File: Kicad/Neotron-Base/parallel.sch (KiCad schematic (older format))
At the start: 11 parts, among them J501 Conn_02x13_Header, U501 MCP23S17_SP

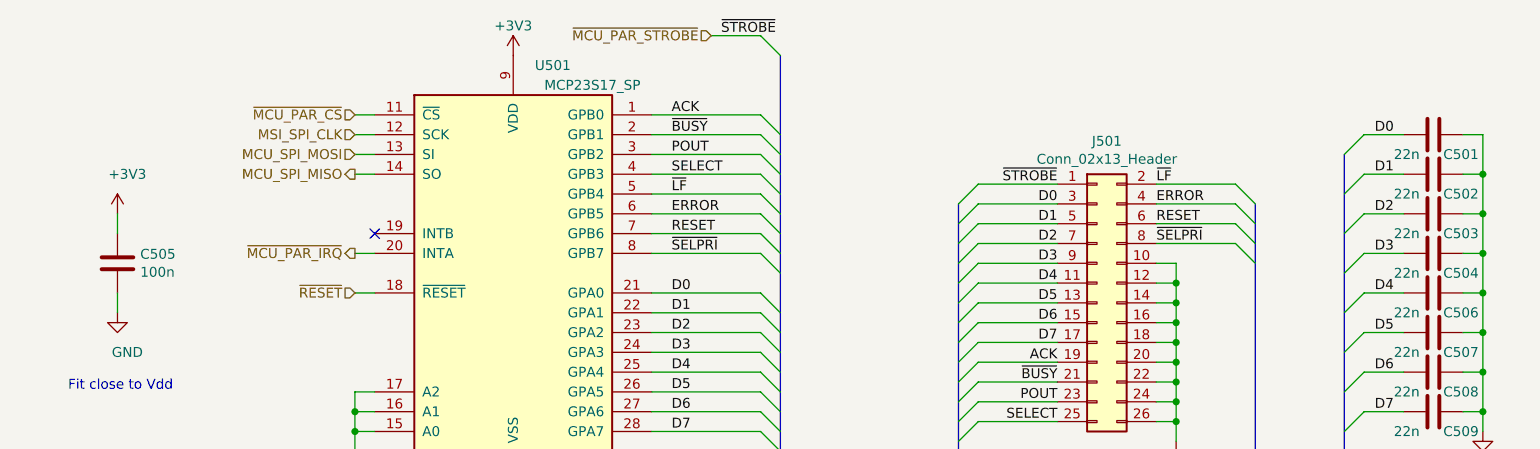
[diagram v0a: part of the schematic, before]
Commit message: Re-work CPU interface to include RMII.
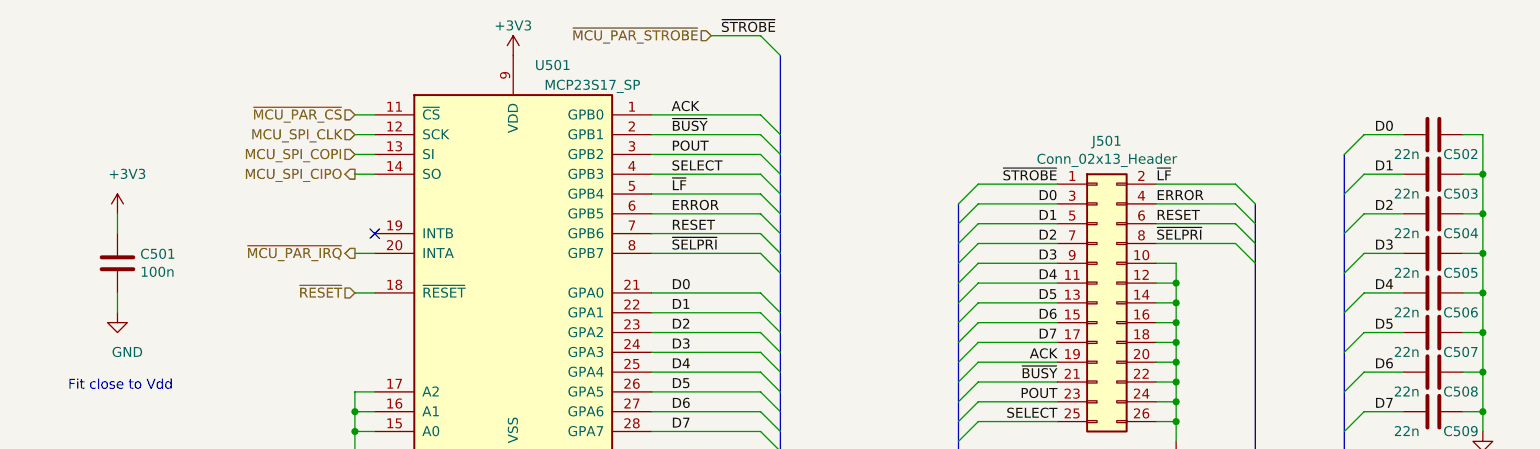
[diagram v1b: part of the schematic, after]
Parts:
- renumbered C505 to C501, C501 to C502, C502 to C503, C503 to C504, C504 to C505
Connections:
- net MCU_SPI_MISO renamed MCU_SPI_CIPO
- net MCU_SPI_MOSI renamed MCU_SPI_COPI
- net MSI_SPI_CLK renamed MCU_SPI_CLK
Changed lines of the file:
@@
 $Descr A4 11693 8268
 encoding utf-8
-Sheet 5 7
+Sheet 5 10
 Title "Neotron Base - Parallel Port"
-Date "2020-08-07"
+Date "2020-08-15"
 Rev "[Uncontrolled]"
 Comp "github.com/neotron-compute"
@@
 ~MCU_PAR_STROBE
 Text HLabel 2650 2900 0    50   Input ~ 0
-MCU_SPI_MOSI
+MCU_SPI_COPI
 Text HLabel 2650 3000 0    50   Output ~ 0
-MCU_SPI_MISO
+MCU_SPI_CIPO
 Text HLabel 2650 2800 0    50   Input ~ 0
-MSI_SPI_CLK
+MCU_SPI_CLK
 Text HLabel 2650 3600 0    50   Input ~ 0
 ~RESET
@@
 $EndComp
 $Comp
-L Device:C C501
+L Device:C C502
 U 1 1 5DFC954B
 P 8100 2800
-F 0 "C501" V 8200 2850 50  0000 L CNN
+F 0 "C502" V 8200 2850 50  0000 L CNN
 F 1 "22n" V 8200 2600 50  0000 L CNN
 F 2 "Capacitor_THT:C_Disc_D3.0mm_W2.0mm_P2.50mm" H 8138 2650 50  0001 C CNN
@@
 $EndComp
 $Comp
-L Device:C C502
+L Device:C C503
 U 1 1 5DFC8D43
 P 8100 3000
-F 0 "C502" V 8200 3050 50  0000 L CNN
+F 0 "C503" V 8200 3050 50  0000 L CNN
 F 1 "22n" V 8200 2800 50  0000 L CNN
 F 2 "Capacitor_THT:C_Disc_D3.0mm_W2.0mm_P2.50mm" H 8138 2850 50  0001 C CNN
@@
 $EndComp
 $Comp
-L Device:C C503
+L Device:C C504
 U 1 1 5DFC8AB4
 P 8100 3200
-F 0 "C503" V 8200 3250 50  0000 L CNN
+F 0 "C504" V 8200 3250 50  0000 L CNN
 F 1 "22n" V 8200 3000 50  0000 L CNN
 F 2 "Capacitor_THT:C_Disc_D3.0mm_W2.0mm_P2.50mm" H 8138 3050 50  0001 C CNN
@@
 $EndComp
 $Comp
-L Device:C C504
+L Device:C C505
 U 1 1 5DFC872D
 P 8100 3400
-F 0 "C504" V 8200 3450 50  0000 L CNN
+F 0 "C505" V 8200 3450 50  0000 L CNN
 F 1 "22n" V 8200 3200 50  0000 L CNN
 F 2 "Capacitor_THT:C_Disc_D3.0mm_W2.0mm_P2.50mm" H 8138 3250 50  0001 C CNN
@@
 AR Path="/5DF1D0B0/5E01C54F" Ref="C?"  Part="1"
 AR Path="/5DF626CD/5E01C54F" Ref="C?"  Part="1"
-AR Path="/5F3C3642/5E01C54F" Ref="C505"  Part="1"
-F 0 "C505" H 1565 3496 50  0000 L CNN
+AR Path="/5F3C3642/5E01C54F" Ref="C501"  Part="1"
+F 0 "C501" H 1565 3496 50  0000 L CNN
 F 1 "100n" H 1565 3405 50  0000 L CNN
 F 2 "Capacitor_THT:C_Disc_D3.0mm_W2.0mm_P2.50mm" H 1488 3300 50  0001 C CNN
